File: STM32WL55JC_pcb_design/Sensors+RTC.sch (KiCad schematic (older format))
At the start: 12 parts

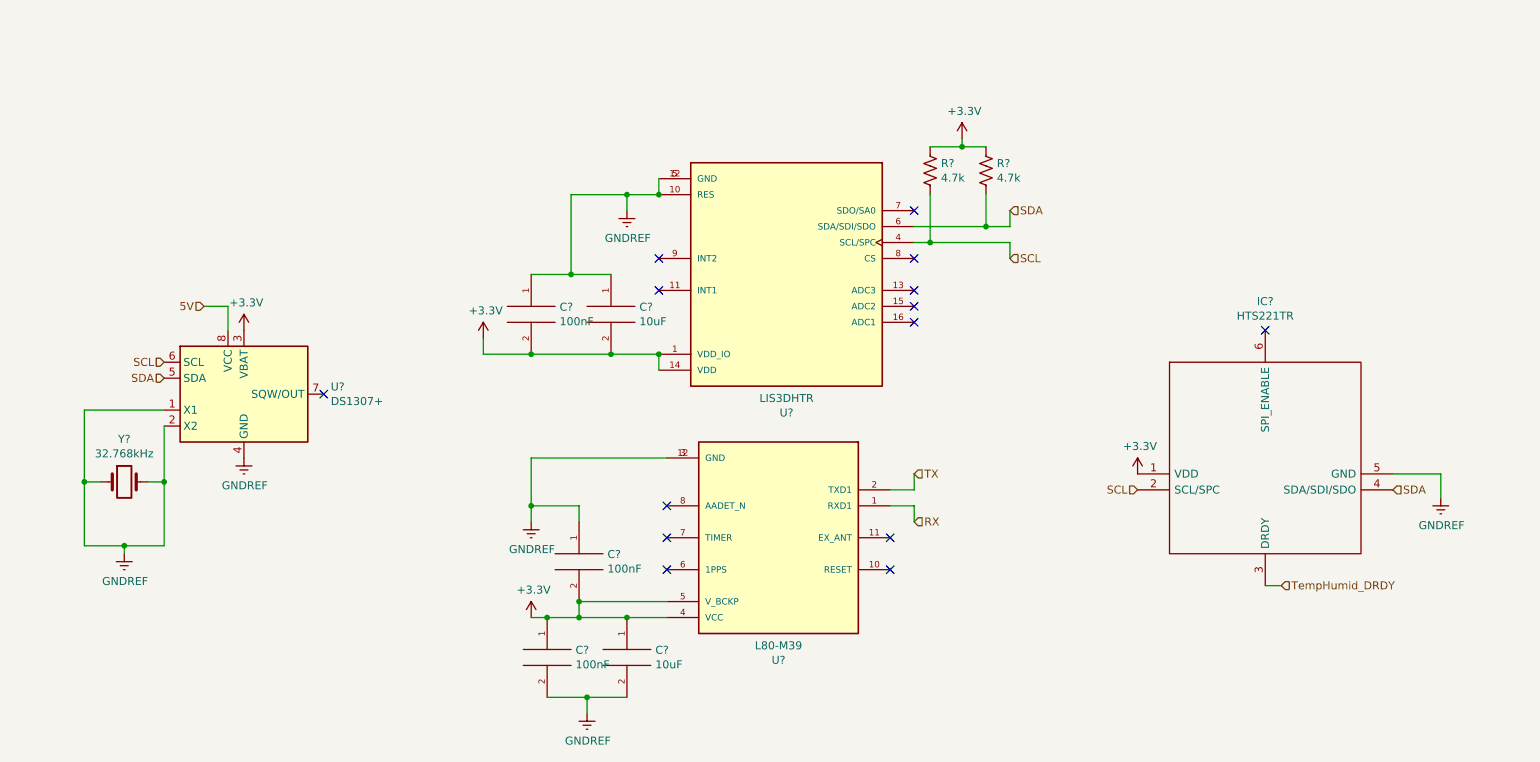
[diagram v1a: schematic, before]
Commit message: Update ADC section to work with MAX11635
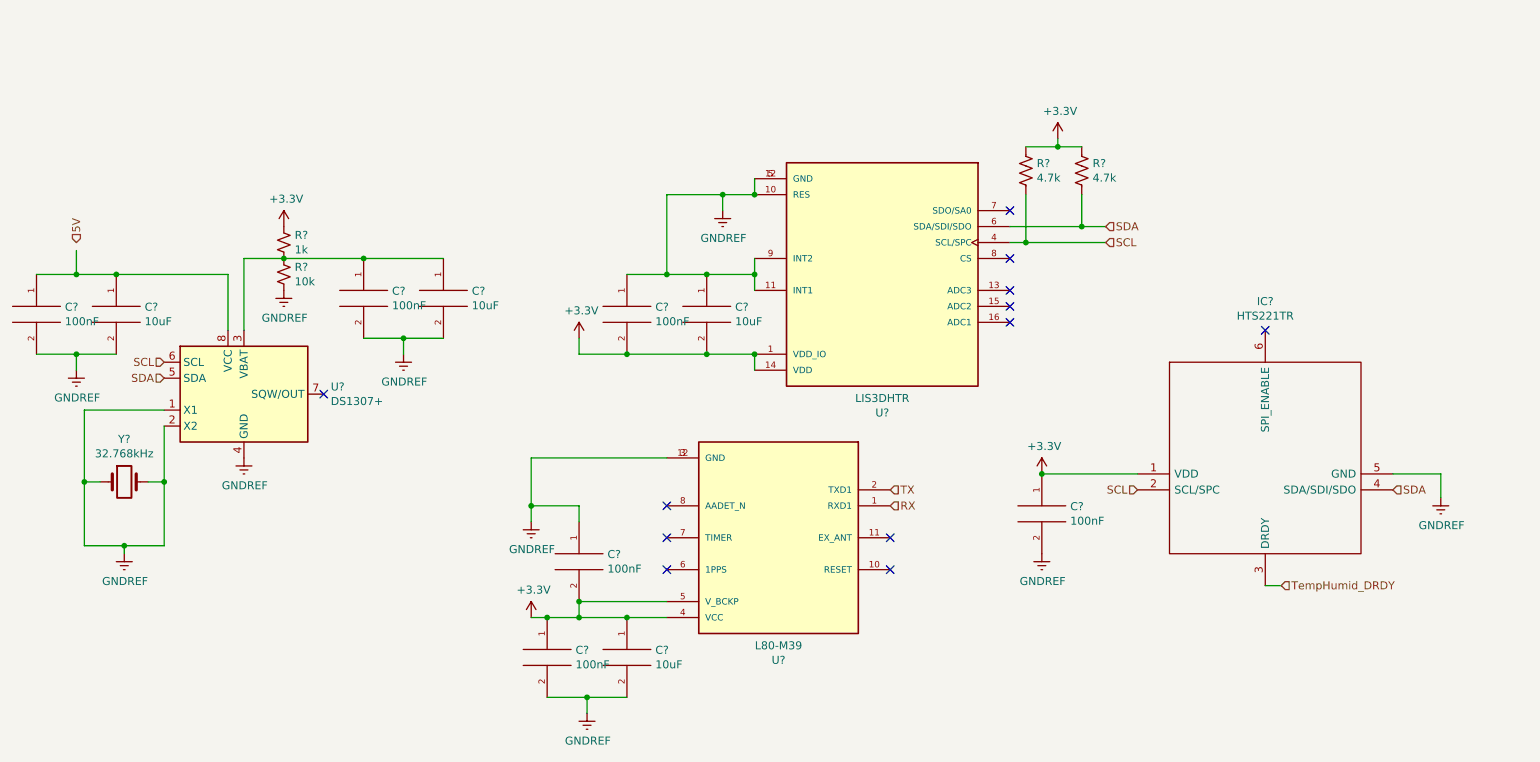
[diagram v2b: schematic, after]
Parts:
- added C? (x2): 10uF, symbol pspice:CAP
- added C? (x3): 100nF, symbol pspice:CAP
- added R?: 1k, symbol Device:R_Small_US
- added R?: 10k, symbol Device:R_Small_US
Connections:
- net +3V3: now also C?.1, R?.1; no longer U?.3 (VBAT)
- net 5V: no longer U?.8 (VCC)
- net GNDREF: now also U?.11 (INT1), U?.9 (INT2), C?.2, C?.2, C?.2, C?.2, C?.2, R?.2
- new net: C?.1, C?.1, R?.1, R?.2, U?.3 (VBAT)
- new net: C?.1, C?.1, U?.8 (VCC)
- no-connect marks 14 -> 12
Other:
- moved on the sheet: C?, R?, U?

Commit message: Finish component selection and footprint assignment
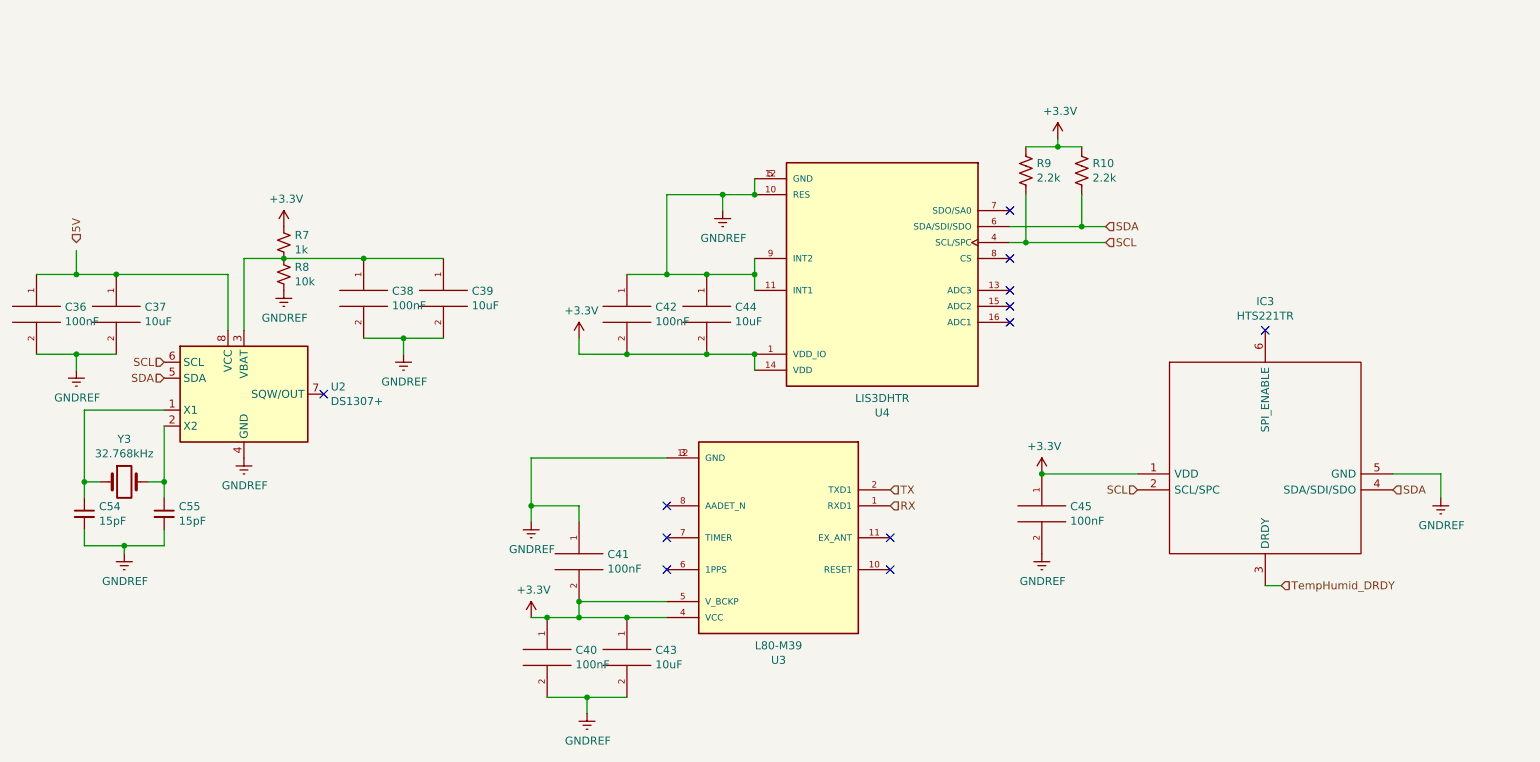
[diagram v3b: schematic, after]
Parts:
- added C54, C55: 15pF, Capacitor_SMD:C_0805_2012Metric, symbol Device:C_Small
- C36, C37, C38, C39, C40, C41, C42, C43, C44, C45: renamed from C?; footprint (none) -> Capacitor_SMD:C_0805_2012Metric
- IC3: renamed from IC?; footprint HLGA-6L -> HTS221TR:HTS221TR
- R10, R9: renamed from R?; value 4.7k -> 2.2k; footprint (none) -> Resistor_SMD:R_0805_2012Metric
- R7, R8: renamed from R?; footprint (none) -> Resistor_SMD:R_0805_2012Metric
- U3: renamed from U?; footprint XCVR_L80-M39 -> L80-M39:XCVR_L80-M39
- U4: renamed from U?; footprint XDCR_LIS3DHTR -> LIS3DHTR:XDCR_LIS3DHTR
- Y3: renamed from Y?; footprint (none) -> SC20S-12.5PF20PPM:SC20S125PF20PPM
- gave numbers to parts that had none: 1
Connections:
- net GNDREF: now also C54.2, C55.2; no longer U2.1 (X1), U2.2 (X2), Y3.1, Y3.2
- new net: C54.1, U2.1 (X1), Y3.1
- new net: C55.1, U2.2 (X2), Y3.2

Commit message: Initial pcb layout
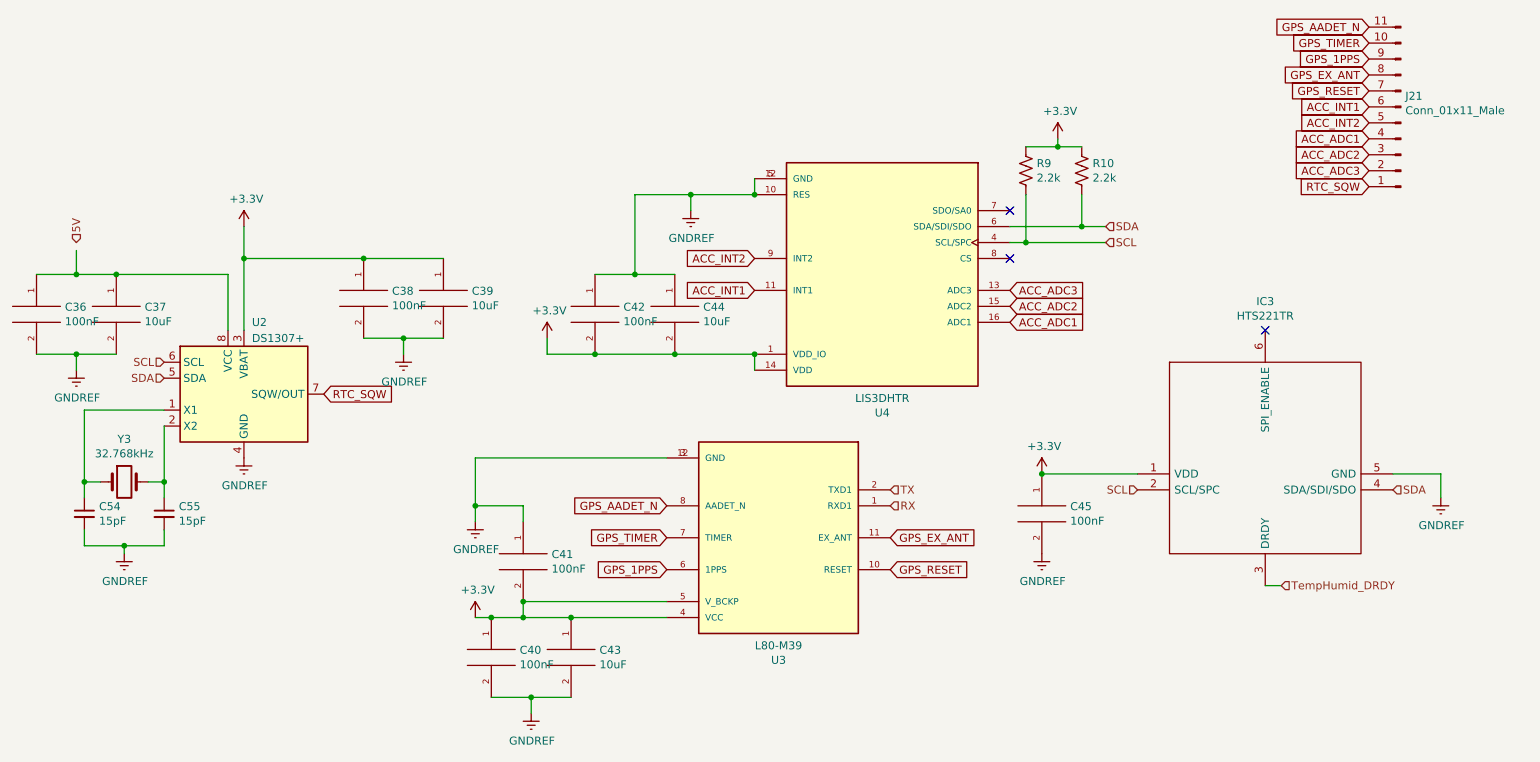
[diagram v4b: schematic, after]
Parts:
- removed R7: 1k, Resistor_SMD:R_0805_2012Metric, symbol Device:R_Small_US
- removed R8: 10k, Resistor_SMD:R_0805_2012Metric, symbol Device:R_Small_US
- added J21: Conn_01x11_Male, Connector_PinHeader_2.54mm:PinHeader_1x11_P2.54mm_Vertical, symbol Connector:Conn_01x11_Male
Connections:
- net +3V3: now also C38.1, C39.1, U2.3 (VBAT)
- net GNDREF: no longer U4.11 (INT1), U4.9 (INT2)
- net GPS_RESET: now reaches U3.10 (RESET)
- net GPS_RESET: now also J21.7 (Pin_7)
- net GPS_EX_ANT: now reaches U3.11 (EX_ANT)
- net GPS_EX_ANT: now also J21.8 (Pin_8)
- net GPS_1PPS: now reaches U3.6 (1PPS)
- net GPS_1PPS: now also J21.9 (Pin_9)
- net GPS_TIMER: now reaches U3.7 (TIMER)
- net GPS_TIMER: now also J21.10 (Pin_10)
- net GPS_AADET_N: now reaches U3.8 (AADET_N)
- net GPS_AADET_N: now also J21.11 (Pin_11)
- net ACC_ADC3: now reaches U4.13 (ADC3)
- net ACC_ADC3: now also J21.2 (Pin_2)
- net ACC_ADC2: now reaches U4.15 (ADC2)
- net ACC_ADC2: now also J21.3 (Pin_3)
- net ACC_ADC1: now reaches U4.16 (ADC1)
- net ACC_ADC1: now also J21.4 (Pin_4)
- net RTC_SQW: now reaches U2.7 (SQW/OUT)
- net RTC_SQW: now also J21.1 (Pin_1)
- new net ACC_INT1: J21.6 (Pin_6), U4.11 (INT1)
- new net ACC_INT2: J21.5 (Pin_5), U4.9 (INT2)
- no-connect marks 12 -> 3
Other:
- moved on the sheet: C40, C41, C42, C43, C44

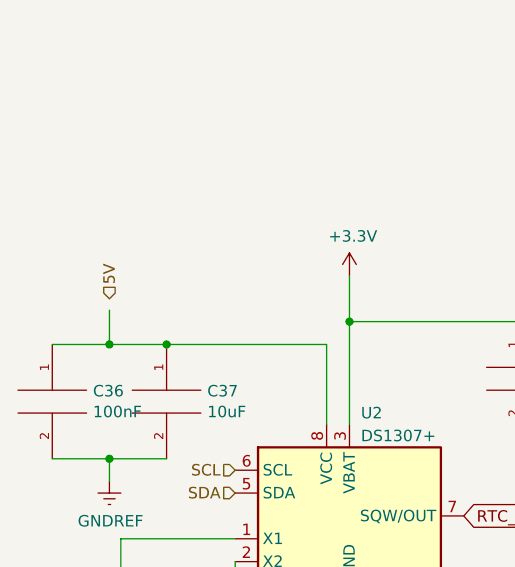
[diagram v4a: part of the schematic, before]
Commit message: Finished component placement
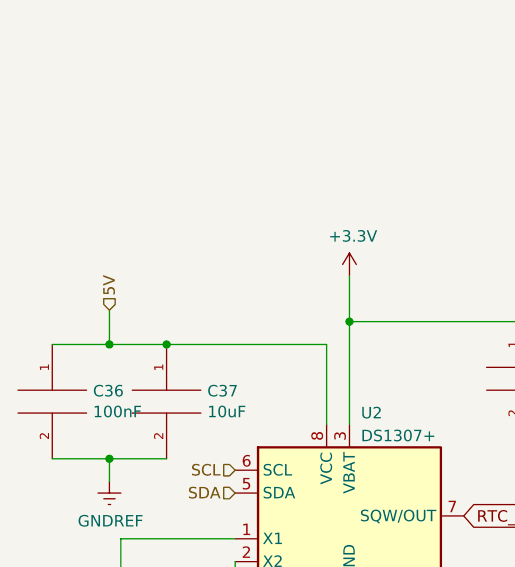
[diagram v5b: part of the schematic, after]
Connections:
- net 5V: now also C36.1, C37.1, U2.8 (VCC)
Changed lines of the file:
@@
 	1    0    0    -1
 $EndComp
-Text HLabel 1350 2600 1    50   Input ~ 0
+Text HLabel 1350 2650 1    50   Input ~ 0
 5V
 $Comp

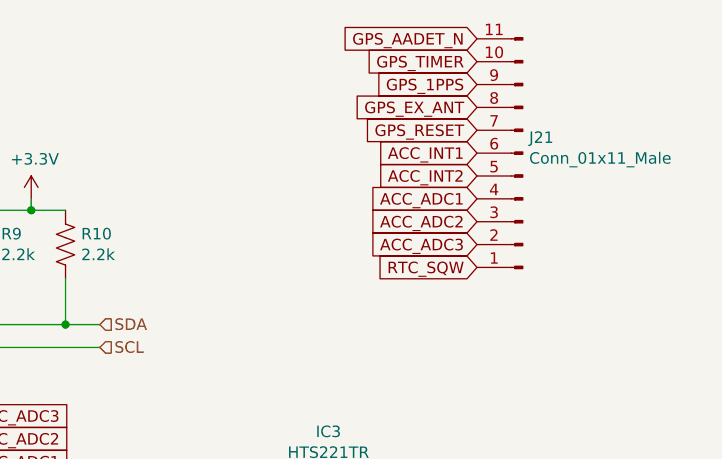
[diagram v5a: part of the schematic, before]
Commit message: Only micro left to be routed
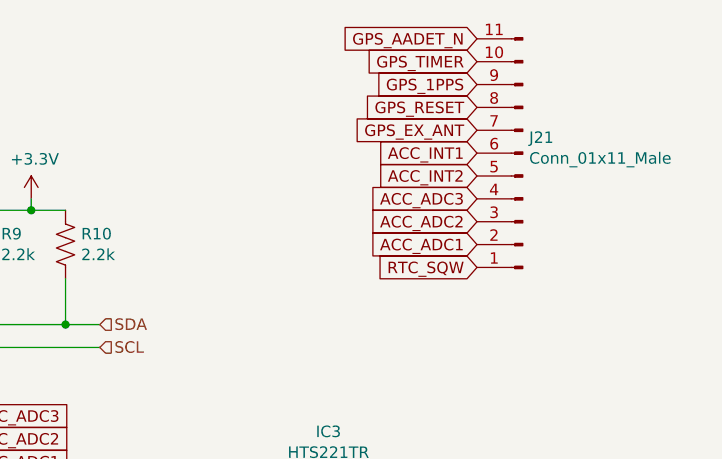
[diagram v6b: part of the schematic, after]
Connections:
- net ACC_ADC1: now also J21.2 (Pin_2); no longer J21.4 (Pin_4)
- net ACC_ADC3: now also J21.4 (Pin_4); no longer J21.2 (Pin_2)
- net GPS_EX_ANT: now also J21.7 (Pin_7); no longer J21.8 (Pin_8)
- net GPS_RESET: now also J21.8 (Pin_8); no longer J21.7 (Pin_7)
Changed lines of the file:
@@
 Text GLabel 9450 1450 0    50   Input ~ 0
 GPS_1PPS
+Text GLabel 9450 1650 0    50   Input ~ 0
+GPS_EX_ANT
 Text GLabel 9450 1550 0    50   Input ~ 0
-GPS_EX_ANT
-Text GLabel 9450 1650 0    50   Input ~ 0
 GPS_RESET
 Text GLabel 7200 2900 2    50   Input ~ 0
@@
 Text GLabel 9450 1850 0    50   Input ~ 0
 ACC_INT2
-Text GLabel 9450 1950 0    50   Input ~ 0
+Text GLabel 9450 2150 0    50   Input ~ 0
 ACC_ADC1
 Text GLabel 9450 2050 0    50   Input ~ 0
 ACC_ADC2
-Text GLabel 9450 2150 0    50   Input ~ 0
+Text GLabel 9450 1950 0    50   Input ~ 0
 ACC_ADC3
 Text GLabel 2900 3550 2    50   Input ~ 0
